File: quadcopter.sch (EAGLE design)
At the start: 60 parts, among them J1 AVR_SPI_PRG_6NS, SW1 PUSHBUTTON_SMD-VERTICAL, SW2 PUSHBUTTON_SMD-VERTICAL, U1 ATMEGA128RFA1

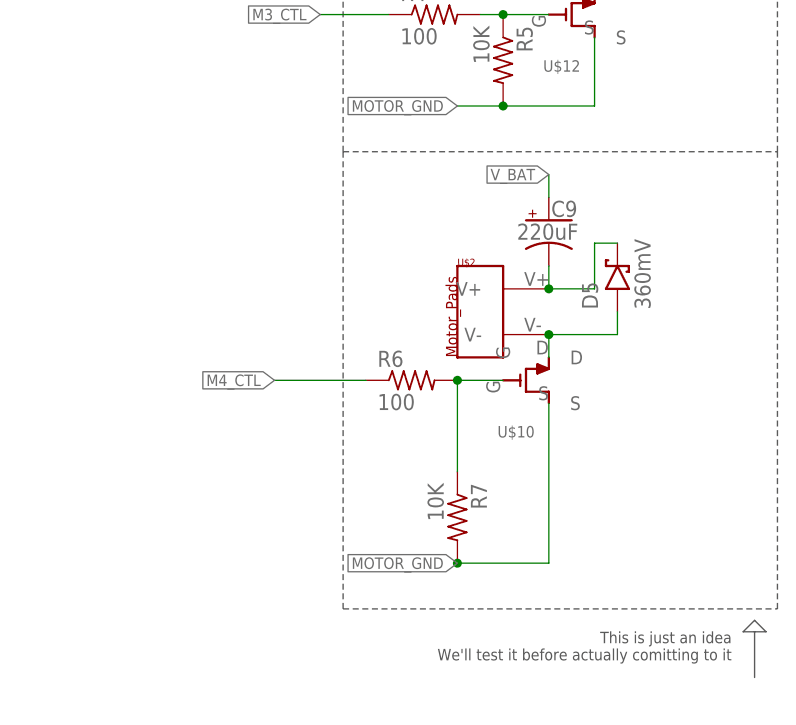
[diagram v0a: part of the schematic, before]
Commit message: updated motor schematic
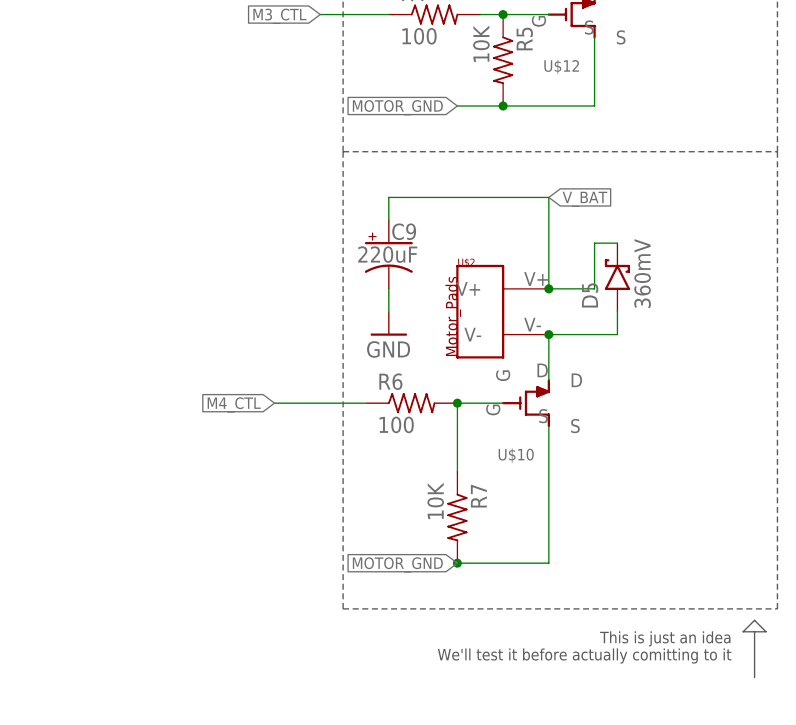
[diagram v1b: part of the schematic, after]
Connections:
- removed net N$15: C9.-, D5.C, U$2.V+
- net GND: now also C9.-
- net V_BAT: now also D5.C, U$2.V+
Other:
- moved on the sheet: C9, R6, U$10
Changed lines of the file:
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@@
 <?xml version="1.0" encoding="utf-8"?>
 <!DOCTYPE eagle SYSTEM "eagle.dtd">
-<eagle version="8.1.0">
+<eagle version="8.1.1">
 <drawing>
 <settings>
@@
 <part name="R17" library="quadparts_prebuilt" deviceset="RESISTOR_" device="SMD-2012-0805-330" value="330"/>
 <part name="GND29" library="quadparts_prebuilt" deviceset="GND" device=""/>
+<part name="GND30" library="quadparts_prebuilt" deviceset="GND" device=""/>
 </parts>
 <sheets>
@@
 <instance part="GND11" gate="1" x="257.81" y="-102.87" rot="R180"/>
 <instance part="GND12" gate="1" x="255.27" y="-146.05" rot="R90"/>
-<instance part="R6" gate="G$1" x="358.14" y="-200.66"/>
+<instance part="R6" gate="G$1" x="358.14" y="-203.2"/>
 <instance part="R7" gate="G$1" x="363.22" y="-215.9" rot="R270"/>
 <instance part="U$2" gate="G$1" x="365.76" y="-195.58"/>
@@
 <instance part="R13" gate="G$1" x="17.78" y="-30.48" rot="R90"/>
 <instance part="GND17" gate="1" x="17.78" y="-40.64"/>
-<instance part="C9" gate="G$1" x="373.38" y="-182.88"/>
+<instance part="C9" gate="G$1" x="355.6" y="-185.42"/>
 <instance part="C10" gate="G$1" x="365.76" y="-139.7"/>
 <instance part="C11" gate="G$1" x="365.76" y="-88.9"/>
@@
 <instance part="U$8" gate="G$1" x="63.5" y="-33.02" rot="R90"/>
 <instance part="U$9" gate="G$1" x="375.92" y="-109.22" rot="MR180"/>
-<instance part="U$10" gate="G$1" x="370.84" y="-200.66" rot="MR180"/>
+<instance part="U$10" gate="G$1" x="370.84" y="-203.2" rot="MR180"/>
 <instance part="U$11" gate="G$1" x="381" y="-58.42" rot="MR180"/>
 <instance part="U$12" gate="G$1" x="375.92" y="-160.02" rot="MR180"/>
@@
 <instance part="R17" gate="G$1" x="167.64" y="-172.72"/>
 <instance part="GND29" gate="1" x="130.81" y="-172.72" rot="R270"/>
+<instance part="GND30" gate="1" x="355.6" y="-195.58"/>
 </instances>
 <busses>
@@
 <pinref part="GND29" gate="1" pin="GND"/>
 <wire x1="148.59" y1="-173.99" x2="133.35" y2="-172.72" width="0.1524" layer="91"/>
+</segment>
+<segment>
+<pinref part="C9" gate="G$1" pin="-"/>
+<wire x1="355.6" y1="-190.5" x2="355.6" y2="-193.04" width="0.1524" layer="91"/>
+<pinref part="GND30" gate="1" pin="GND"/>
 </segment>
 </net>
@@
 <wire x1="373.38" y1="-220.98" x2="363.22" y2="-220.98" width="0.1524" layer="91"/>
 <pinref part="U$10" gate="G$1" pin="S"/>
-<wire x1="373.38" y1="-203.2" x2="373.38" y2="-220.98" width="0.1524" layer="91"/>
+<wire x1="373.38" y1="-205.74" x2="373.38" y2="-220.98" width="0.1524" layer="91"/>
 </segment>
 <segment>
@@
 </segment>
 <segment>
-<label x="373.38" y="-177.8" size="1.27" layer="95" font="fixed" rot="R180" xref="yes"/>
-<wire x1="373.38" y1="-180.34" x2="373.38" y2="-177.8" width="0.1524" layer="91"/>
 <pinref part="C9" gate="G$1" pin="+"/>
+<wire x1="355.6" y1="-182.88" x2="355.6" y2="-180.34" width="0.1524" layer="91"/>
+<pinref part="U$2" gate="G$1" pin="V+"/>
+<wire x1="373.38" y1="-190.5" x2="378.46" y2="-190.5" width="0.1524" layer="91"/>
+<wire x1="378.46" y1="-190.5" x2="378.46" y2="-185.42" width="0.1524" layer="91"/>
+<pinref part="D5" gate="G$1" pin="C"/>
+<wire x1="378.46" y1="-185.42" x2="381" y2="-185.42" width="0.1524" layer="91"/>
+<wire x1="355.6" y1="-180.34" x2="373.38" y2="-180.34" width="0.1524" layer="91"/>
+<wire x1="373.38" y1="-180.34" x2="373.38" y2="-190.5" width="0.1524" layer="91"/>
+<junction x="373.38" y="-190.5"/>
+<label x="373.38" y="-180.34" size="1.27" layer="95" font="fixed" xref="yes"/>
 </segment>
 </net>
@@
 <segment>
 <pinref part="R6" gate="G$1" pin="1"/>
-<wire x1="353.06" y1="-200.66" x2="342.9" y2="-200.66" width="0.1524" layer="91"/>
-<label x="342.9" y="-200.66" size="1.27" layer="95" font="fixed" rot="MR0" xref="yes"/>
+<wire x1="353.06" y1="-203.2" x2="342.9" y2="-203.2" width="0.1524" layer="91"/>
+<label x="342.9" y="-203.2" size="1.27" layer="95" font="fixed" rot="MR0" xref="yes"/>
 </segment>
 <segment>
@@
 <pinref part="R6" gate="G$1" pin="2"/>
 <pinref part="R7" gate="G$1" pin="1"/>
-<wire x1="363.22" y1="-210.82" x2="363.22" y2="-200.66" width="0.1524" layer="91"/>
-<wire x1="363.22" y1="-200.66" x2="368.3" y2="-200.66" width="0.1524" layer="91"/>
-<junction x="363.22" y="-200.66"/>
+<wire x1="363.22" y1="-210.82" x2="363.22" y2="-203.2" width="0.1524" layer="91"/>
+<wire x1="363.22" y1="-203.2" x2="368.3" y2="-203.2" width="0.1524" layer="91"/>
+<junction x="363.22" y="-203.2"/>
 <pinref part="U$10" gate="G$1" pin="G"/>
 </segment>
@@
 <pinref part="U$2" gate="G$1" pin="V-"/>
 <pinref part="U$10" gate="G$1" pin="D"/>
-<wire x1="373.38" y1="-195.58" x2="373.38" y2="-198.12" width="0.1524" layer="91"/>
+<wire x1="373.38" y1="-195.58" x2="373.38" y2="-200.66" width="0.1524" layer="91"/>
 <wire x1="373.38" y1="-195.58" x2="381" y2="-195.58" width="0.1524" layer="91"/>
 <junction x="373.38" y="-195.58"/>
@@
 </segment>
 </net>
-<net name="N$15" class="0">
-<segment>
-<pinref part="C9" gate="G$1" pin="-"/>
-<pinref part="U$2" gate="G$1" pin="V+"/>
-<wire x1="373.38" y1="-187.96" x2="373.38" y2="-190.5" width="0.1524" layer="91"/>
-<wire x1="373.38" y1="-190.5" x2="378.46" y2="-190.5" width="0.1524" layer="91"/>
-<wire x1="378.46" y1="-190.5" x2="378.46" y2="-185.42" width="0.1524" layer="91"/>
-<junction x="373.38" y="-190.5"/>
-<pinref part="D5" gate="G$1" pin="C"/>
-<wire x1="378.46" y1="-185.42" x2="381" y2="-185.42" width="0.1524" layer="91"/>
-</segment>
-</net>

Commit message: Fixed spacing issue and reset issue
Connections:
- net GND: no longer R3.2
- net VCC: now also R3.2
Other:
- moved on the sheet: B1, BATT1, C1, C10, C11, C12, C13, C14, C15, C2, C3, C4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

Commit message: started board
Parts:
- added C16, C17, C18, C19, C20, C21, C24, C25: 1uF, quadparts_prebuilt:CAPACITOR-NP_SMD-2012-0805_CERAMIC-1UF
- added C22, C23: 12pF, quadparts_prebuilt:CAPACITOR-NP_SMD-2012-0805_CERAMIC-12PF
- added Y1: (no value), quadparts_prebuilt:CRYSTAL5X3
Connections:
- new net N$15: C22.1, U1.XTAL1, Y1.2
- new net N$19: C23.1, U1.XTAL2, Y1.1
- new net N$20: C24.1, U1.DVDD
- new net N$21: C25.1, U1.AVDD
- net GND: now also C16.2, C17.1, C22.2, C23.2, C24.2, C25.2
- net M1_CTL: now also C18.1
- net M2_CTL: now also C19.1
- net M3_CTL: now also C20.1
- net M4_CTL: now also C21.1
- net MOTOR_GND: now also C19.2, C20.2, C21.2
- net VCC: now also C17.2
- net V_BAT: now also C16.1
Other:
- moved on the sheet: BATT1, LED_Y, R12, R13, R17, U$6, U$8

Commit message: started laying out basic board
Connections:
- net MOTOR_GND: now also C18.2
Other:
- moved on the sheet: C10, C11, C12, C18, C19, C20, C21, C9, D5, D6, D7, D8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

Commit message: basic board layout added
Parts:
- removed C15: 0.1uF, quadparts_prebuilt:CAPACITOR-NP_SMD-2012-0805_CERAMIC-0.1UF
- added J3, J4, J5, J6: HEADER-0.1IN-2POS-FEMALE, Components:HEADER-0.1IN-2POS-FEMALE
- added J7: (no value), Components:HEADER-0.1IN-3POS-MALE
- J2: device quadparts_prebuilt:SIP-10_TH-254X10-1 -> Components:HEADER-0.1IN-5POS-FEMALE
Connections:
- removed net N$16: C15.2, JP2.1
- removed net VBAT: J2.10
- new net NOT_CONNECTED: J2.2
- net GND: now also J2.4, J7.2; no longer J2.2
- net M1_CTL: now also J3.2; no longer J2.8
- net M2_CTL: now also J4.2; no longer J2.7
- net M3_CTL: now also J5.2; no longer J2.6
- net M4_CTL: now also J6.2; no longer J2.5
- net MOTOR_GND: now also J3.1, J4.1, J5.1, J6.1; no longer J2.9
- net RESET: no longer C15.1
- net SCL: now also J2.3; no longer J2.4
- net SDA: now also J2.1; no longer J2.3
- net VCC: now also J2.5, J7.3; no longer J2.1
- net V_BAT: now also J7.1
